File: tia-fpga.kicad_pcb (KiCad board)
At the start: 2 copper layers, 70 x 32 mm, 23 parts, among them J1 PinSocket_1x24_P2.54mm_Vertic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, J2 PinHeader_1x20_P2.54mm_Vertic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, J3 PinHeader_1x20_P2.54mm_Vertic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, J4 PinSocket_1x24_P2.54mm_Vertic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, U1 SOIC-14_3.9x8.7mm_P1.27mm, U2 SOIC-20W_7.5x12.8mm_P1.27mm, U3 SOIC-20W_7.5x12.8mm_P1.27mm, U4 SOIC-20W_7.5x12.8mm_P1.27mm, U5 SOT-23-5, U6 74LVC2G07, U7 74LVC2G07, U8 74LVC2G07, U9 74LVC2G07

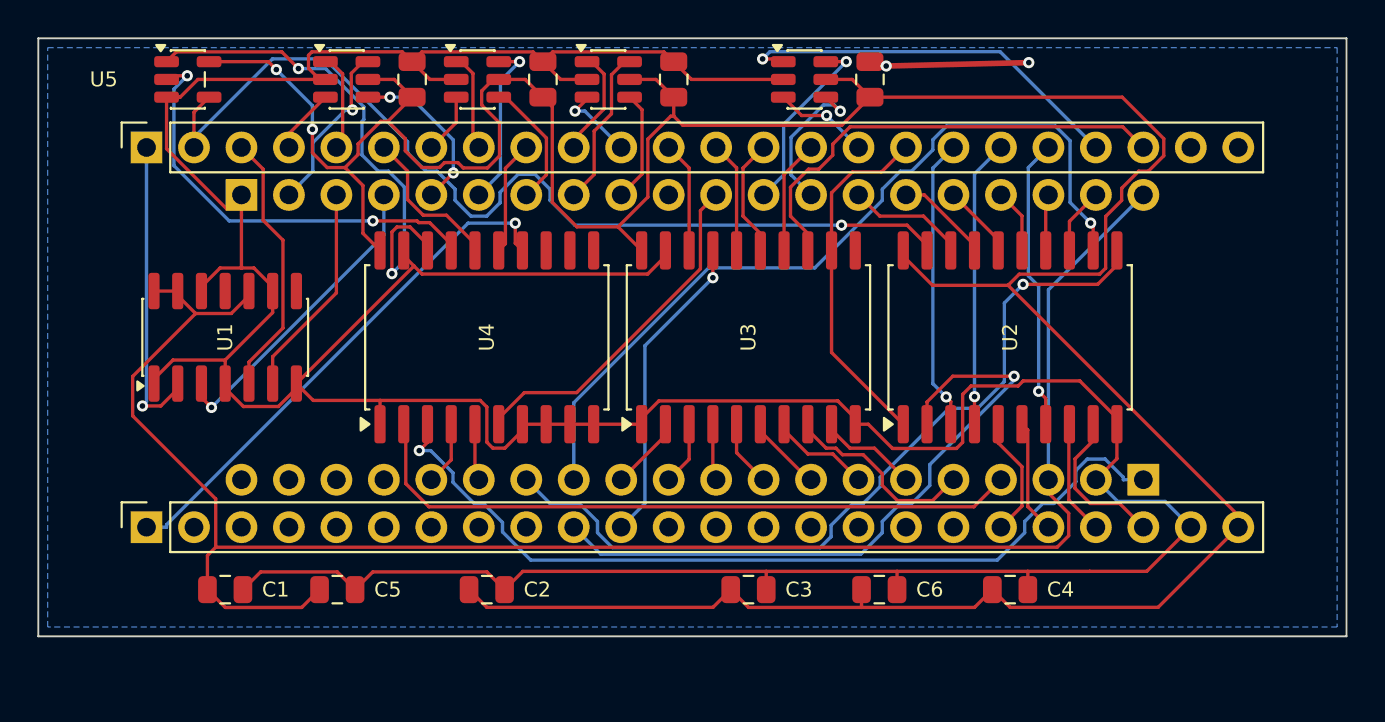
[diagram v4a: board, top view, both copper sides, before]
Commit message: Fix the Tang Nano interface: row spacing, row order, 5 V
Sipeed's dimension drawing for the Tang Nano 9K settles two things this board
had guessed. The module's header rows are 22.86 mm apart, not 20.32, and seen
from above with the USB-C end on the left its J6 row is the upper one -- so the
sockets were the wrong way round as well. J1 now takes J6 and J4 takes J5.
Three sources agree on the order: the pin numbers on the module's underside,
the QN88's own pin order in the top-side photo of Sipeed's datasheet, and
third-party carrier boards for the module. Rev A had both errors too; nothing
was ever fabricated from either.

J1/18, the module's 5 V input, was left open on purpose for breadboard use,
with the Tang Nano powered over USB. In a console that would mean a USB supply
inside the case, so D1 (MBR0540, SOD-123) now feeds it from the TIA socket's
+5 V and blocks the module's USB from feeding the console back.

The board grows 2.54 mm, to 70 x 34.54 mm: J4 moves to y = 28.70 and the
channel's decoupling moves with it, which leaves the top margin as it was. The
pin assignment was solved again for the new geometry (571 mm summed, F_OSC
still on J6/1, the PLL's own input) and the board re-routed: 561 segments, 37
vias, 1.52 m of copper. Freerouting left two ground branches open; each is
closed with a via dropped on the track itself, where it passes over the main
island of the pour. ERC 0; DRC 0 violations, 0 unconnected pads.

Boot time: the console releases the 6507's reset 17 to 58 ms after power-up,
depending on the board revision, and PHI0 has to be running by then. At Gowin's
default 2.5 MHz the GW1NR-9 takes about 100 ms to load its bitstream from
flash, so build_gowin.tcl now asks for -loading_rate 250/8 (31.25 MHz, the
fastest the device allows in Autoboot): about 8 ms. Timing still closes, at
60.4 MHz against the 57.27 MHz clock.

Gerbers, drill, PDFs, renders, both BOMs and the README follow the board.

Co-Authored-By: Claude Opus 5 <noreply@anthropic.com>
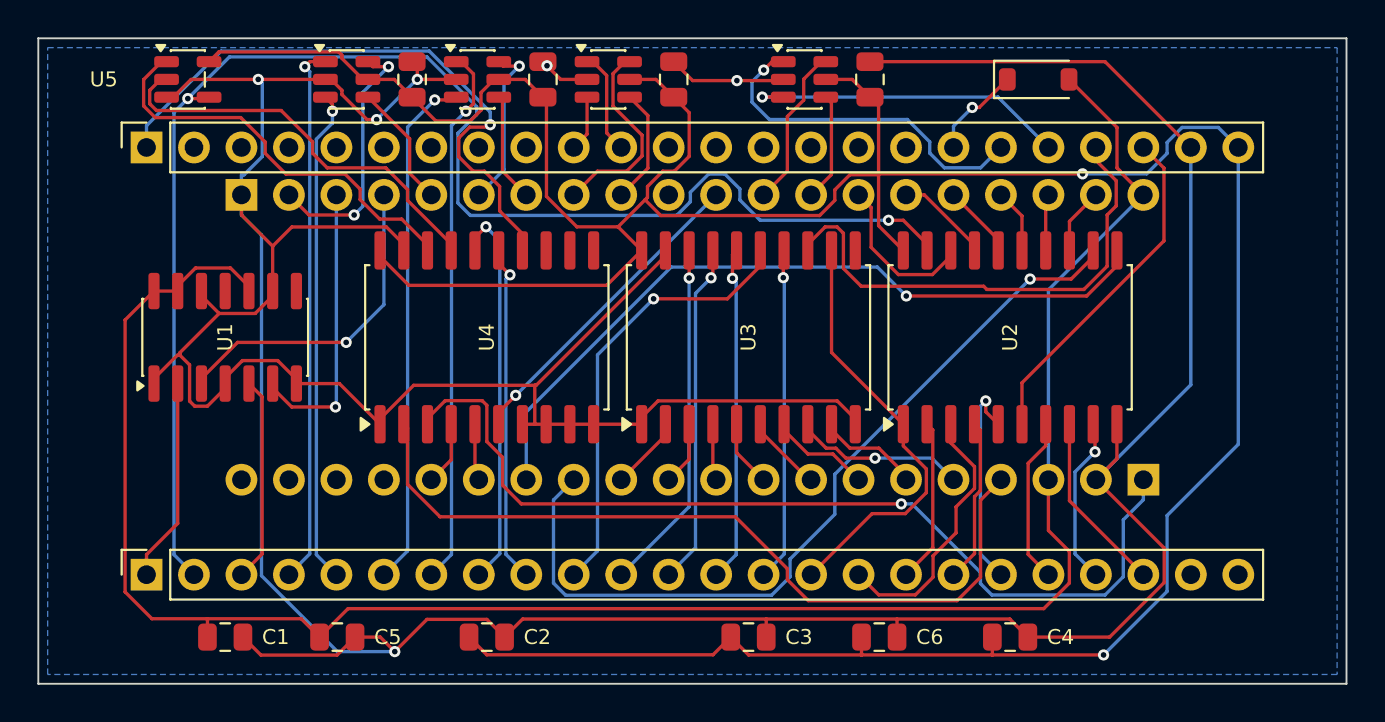
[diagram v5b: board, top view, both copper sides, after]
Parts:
- added D1: MBR0540, D_SOD-123, F.Cu at (53.5, 2.20)
- moved C1 2.54 mm to (10.0, 32.0)
- moved C2 2.54 mm to (24.0, 32.0)
- moved C3 2.54 mm to (38.0, 32.0)
- moved C4 2.54 mm to (52.0, 32.0)
- moved C5 2.54 mm to (16.0, 32.0)
- moved C6 2.54 mm to (45.0, 32.0)
- moved J4 2.54 mm to (5.79, 28.7)
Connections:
- J1 pad 1: /F_PHI0 -> /F_OSC
- J1 pad 10: /F_LUM0 -> /F_COL
- J1 pad 11: /F_COL -> /F_LUM0
- J1 pad 12: /F_A0 -> unconnected-(J1-Pin_12-Pad12)
- J1 pad 13: /F_A2 -> unconnected-(J1-Pin_13-Pad13)
- J1 pad 14: /F_A3 -> unconnected-(J1-Pin_14-Pad14)
- J1 pad 15: /F_A4 -> unconnected-(J1-Pin_15-Pad15)
- J1 pad 16: /F_AU0 -> unconnected-(J1-Pin_16-Pad16)
- J1 pad 17: /F_RW -> unconnected-(J1-Pin_17-Pad17)
- J1 pad 18: /F_D1 -> /TN_5V
- J1 pad 19: /F_D2 -> /F_AU1
- J1 pad 2: /F_CS_N -> unconnected-(J1-Pin_2-Pad2)
- J1 pad 20: /F_D5 -> /F_AU0
- J1 pad 21: /F_AU1 -> /F_A5
- J1 pad 22: /F_A5 -> /F_D4
- J1 pad 23: unconnected-(J1-Pin_23-Pad23) -> GND
- J1 pad 24: unconnected-(J1-Pin_24-Pad24) -> +3V3
- J1 pad 3: /F_RDY -> unconnected-(J1-Pin_3-Pad3)
- J1 pad 4: /F_LUM1 -> unconnected-(J1-Pin_4-Pad4)
- J1 pad 5: /F_CSYNC -> unconnected-(J1-Pin_5-Pad5)
- J1 pad 6: /F_I4 -> unconnected-(J1-Pin_6-Pad6)
- J1 pad 7: /F_LUM2 -> unconnected-(J1-Pin_7-Pad7)
- J1 pad 8: /F_BLK -> unconnected-(J1-Pin_8-Pad8)
- J1 pad 9: /F_I5 -> unconnected-(J1-Pin_9-Pad9)
- J4 pad 1: /F_OSC -> /F_PHI0
- J4 pad 10: /F_D0 -> /F_A3
- J4 pad 11: /F_A1 -> /F_A0
- J4 pad 12: unconnected-(J4-Pin_12-Pad12) -> /F_A1
- J4 pad 13: unconnected-(J4-Pin_13-Pad13) -> /F_A2
- J4 pad 14: unconnected-(J4-Pin_14-Pad14) -> /F_A4
- J4 pad 15: unconnected-(J4-Pin_15-Pad15) -> /F_RW
- J4 pad 16: unconnected-(J4-Pin_16-Pad16) -> /F_D1
- J4 pad 17: unconnected-(J4-Pin_17-Pad17) -> /F_D0
- J4 pad 18: unconnected-(J4-Pin_18-Pad18) -> /F_D2
- J4 pad 2: unconnected-(J4-Pin_2-Pad2) -> /F_CS_N
- J4 pad 20: /F_D4 -> /F_D5
- J4 pad 21: /F_D6 -> /F_D7
- J4 pad 22: /F_D7 -> /F_D6
- J4 pad 23: GND -> unconnected-(J4-Pin_23-Pad23)
- J4 pad 24: +3V3 -> unconnected-(J4-Pin_24-Pad24)
- J4 pad 3: unconnected-(J4-Pin_3-Pad3) -> /F_RDY
- J4 pad 4: unconnected-(J4-Pin_4-Pad4) -> /F_CSYNC
- J4 pad 5: unconnected-(J4-Pin_5-Pad5) -> /F_LUM1
- J4 pad 6: unconnected-(J4-Pin_6-Pad6) -> /F_LUM2
- J4 pad 7: unconnected-(J4-Pin_7-Pad7) -> /F_BLK
- J4 pad 8: unconnected-(J4-Pin_8-Pad8) -> /F_I4
- J4 pad 9: unconnected-(J4-Pin_9-Pad9) -> /F_I5
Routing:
- net /F_CS_N: track 52.2 -> 79.3 mm, vias 1 -> 2
- net /F_D0: track 35.7 -> 8.77 mm, vias 1 -> 0
- net /F_LUM2: track 3.24 -> 27.7 mm, vias 0 -> 1
- net /F_CSYNC: track 5.27 -> 29.0 mm, vias 0 -> 1
- net /F_BLK: track 5.25 -> 28.9 mm, vias 0 -> 1
- net /F_LUM1: track 3.50 -> 26.5 mm, vias 0 -> 1
- net GND: track 229.5 -> 250.2 mm, vias 2 -> 6
- net /F_A3: track 6.35 -> 23.8 mm, vias 0 -> 1
- net /F_A0: track 5.96 -> 18.9 mm, vias 0 -> 1
- net /F_I4: track 8.26 -> 20.9 mm, vias 0 -> 1
- net /F_AU0: track 5.14 -> 17.6 mm
- net /F_D4: track 6.10 -> 18.4 mm
- net /F_I5: track 6.12 -> 18.1 mm, vias 0 -> 1
- net /F_A2: track 5.96 -> 18.0 mm, vias 0 -> 1
- net /F_A4: track 6.11 -> 17.8 mm, vias 0 -> 1
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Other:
- board size 70 x 32 mm -> 70 x 34.5 mm

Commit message: Centre the TIA rows and trim the board to 61.6 mm
The DIP rows sat 1.27 mm off the centre between the module's sockets, left
over from growing the board downwards, and the ends carried more board than
the sockets need. J2, J3 and the channel logic move down 1.27 mm, which leaves
3.81 mm of gap on each side, and the outline loses 8.4 mm: 61.6 x 34.54 mm,
with 0.74 mm of copper to the edge at the ends of the sockets. The board now
reaches about 6.5 mm past the TIA's own pins instead of 10.9.

Re-routed at the new geometry: 534 segments, 39 vias, 1.48 m of copper. The
router left three ground connections open; two took a via on the branch's own
track where it passes over the pour, and the last two capacitors are tied to
their neighbours along the free lane just inside the top edge. The pour is
smaller and in two islands now (759 mm2), since the board is narrower and the
routing denser, but every ground item is connected. U5's designator moves to
the back silkscreen, where the other top-margin parts already keep theirs.
ERC 0; DRC 0 violations, 0 unconnected pads.

Gerbers, drill, the PCB PDF, renders, the fabrication notes and the README
follow the board.

Co-Authored-By: Claude Opus 5 <noreply@anthropic.com>
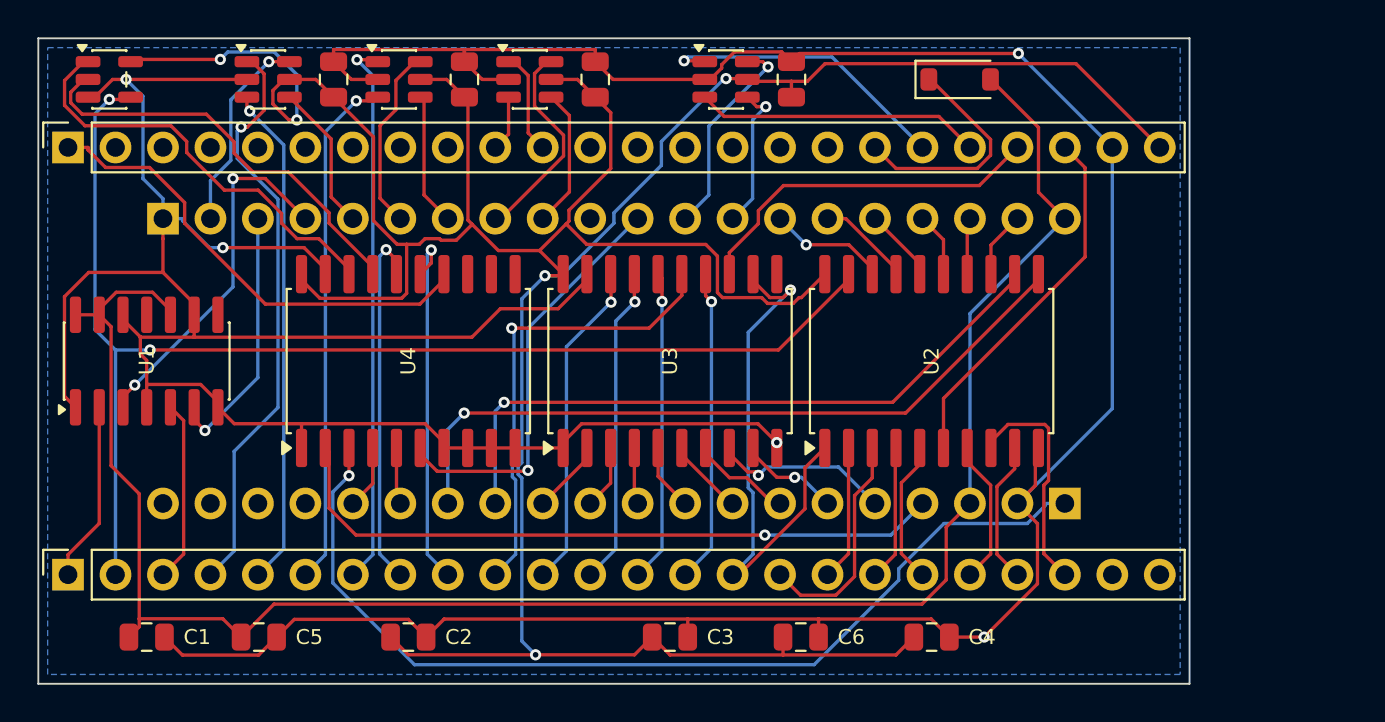
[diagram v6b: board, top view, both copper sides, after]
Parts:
- moved J3 4.39 mm to (54.9, 24.9)
- moved U2 4.39 mm to (47.8, 17.3)
- moved U3 4.39 mm to (33.8, 17.3)
- moved U1 4.39 mm to (5.80, 17.3)
- moved J2 4.39 mm to (6.67, 9.65)
- moved U4 4.39 mm to (19.8, 17.3)
- moved C10 4.20 mm to (40.3, 2.20)
- moved C3 4.20 mm to (33.8, 32.0)
- moved C4 4.20 mm to (47.8, 32.0)
- moved C6 4.20 mm to (40.8, 32.0)
- moved D1 4.20 mm to (49.3, 2.20)
- moved U9 4.20 mm to (36.8, 2.20)
- moved C1 4.20 mm to (5.80, 32.0)
- moved J1 4.20 mm to (1.59, 5.84)
- moved J4 4.20 mm to (1.59, 28.7)
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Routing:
- net /F_CS_N: track 79.3 -> 68.5 mm
- net /TIA_D6: track 44.8 -> 36.0 mm
- net /F_OSC: track 33.0 -> 25.2 mm, vias 1 -> 0
- net /F_A5: track 26.7 -> 19.3 mm
- net /TN_5V: track 5.05 -> 12.4 mm, vias 1 -> 0
- net +5V: track 108.0 -> 100.7 mm
- net /TIA_CS0_N: track 43.1 -> 36.4 mm, vias 0 -> 1
- net +3V3: track 175.0 -> 181.5 mm, vias 2 -> 5
- net /F_RW: track 23.0 -> 28.7 mm, vias 0 -> 1
- net /TIA_OSC: track 17.1 -> 22.4 mm
- net /F_D3: track 11.4 -> 7.66 mm, vias 1 -> 0
- net /TIA_CSYNC: track 13.8 -> 10.8 mm, vias 2 -> 1
- net /F_AU1: track 18.8 -> 16.0 mm
- net /F_D6: track 9.69 -> 12.3 mm
- net /TIA_AU1: track 8.65 -> 11.2 mm, vias 0 -> 1
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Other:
- board size 70 x 34.5 mm -> 61.6 x 34.5 mm

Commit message: Put the licence notice on the back silkscreen
CERN-OHL-S v2 asks for the notice to travel with the board, and until now it
lived only in the files. The back silkscreen carries CERN-OHL-S v2, LRRosa 2026
and github.com/lrrosa/tia-fpga, centred between the two rows of TIA pins, where
the back had neither silk nor pads.

DRC stays at 0 violations and 0 unconnected pads. Gerbers, drill, the PCB PDF
and both renders follow; the fabrication notes and the README ask for the
notice to be kept on a respin.

Co-Authored-By: Claude Opus 5 <noreply@anthropic.com>
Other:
- board text added: "CERN-OHL-S v2"
- board text added: "LRRosa 2026"
- board text added: "github.com/lrrosa/tia-fpga"
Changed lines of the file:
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@@
 		(layer "Edge.Cuts")
+	)
+	(gr_text "github.com/lrrosa/tia-fpga"
+		(at 30.8 20.54 0)
+		(layer "B.SilkS")
+		(effects
+			(font
+				(size 1.3 1.3)
+				(thickness 0.2)
+			)
+			(justify mirror)
+		)
+	)
+	(gr_text "LRRosa 2026"
+		(at 30.8 14 0)
+		(layer "B.SilkS")
+		(effects
+			(font
+				(size 1.4 1.4)
+				(thickness 0.2)
+			)
+			(justify mirror)
+		)
+	)
+	(gr_text "CERN-OHL-S v2"
+		(at 30.8 17.27 0)
+		(layer "B.SilkS")
+		(effects
+			(font
+				(size 1.4 1.4)
+				(thickness 0.2)
+			)
+			(justify mirror)
+		)
 	)
 	(segment

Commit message: Mark pin 1 and the keyed end on the silkscreen
The board went out with no way to tell which end of the DIP row is pin 1. The
back now carries a half moon at the end where the TIA's pin 1 and pin 40 sit,
keyed the way the chip's own package is, and the numbers 1, 20, 21 and 40
beside the corner pads; the front repeats 1 and 40. The front cannot take the
half moon: U1's own outline is in that corner.

DRC stays at 0 violations and 0 unconnected pads. Gerbers, drill, the PCB PDF,
both renders, the fabrication notes and the README follow.

Co-Authored-By: Claude Opus 5 <noreply@anthropic.com>
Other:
- board text added: "1"
- board text added: "20"
- board text added: "21"
- board text added: "40"
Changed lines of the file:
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@@
+	)
+	(gr_line
+		(start 0.947703 17.632346)
+		(end 0.899999 17.27)
+		(stroke
+			(width 0.15)
+			(type default)
+		)
+		(layer "B.SilkS")
+	)
+	(gr_line
+		(start 1.087564 17.97)
+		(end 0.947703 17.632346)
+		(stroke
+			(width 0.15)
+			(type default)
+		)
+		(layer "B.SilkS")
+	)
+	(gr_line
+		(start 1.31005 18.259949)
+		(end 1.087564 17.97)
+		(stroke
+			(width 0.15)
+			(type default)
+		)
+		(layer "B.SilkS")
+	)
+	(gr_line
+		(start 1.599999 18.482435)
+		(end 1.31005 18.259949)
+		(stroke
+			(width 0.15)
+			(type default)
+		)
+		(layer "B.SilkS")
+	)
+	(gr_line
+		(start 1.937653 18.622296)
+		(end 1.599999 18.482435)
+		(stroke
+			(width 0.15)
+			(type default)
+		)
+		(layer "B.SilkS")
+	)
+	(gr_line
+		(start 2.3 18.67)
+		(end 1.937653 18.622296)
+		(stroke
+			(width 0.15)
+			(type default)
+		)
+		(layer "B.SilkS")
+	)
+	(gr_line
+		(start 2.662346 18.622296)
+		(end 2.3 18.67)
+		(stroke
+			(width 0.15)
+			(type default)
+		)
+		(layer "B.SilkS")
+	)
+	(gr_line
+		(start 2.999999 18.482435)
+		(end 2.662346 18.622296)
+		(stroke
+			(width 0.15)
+			(type default)
+		)
+		(layer "B.SilkS")
+	)
+	(gr_line
+		(start 3.289949 18.259949)
+		(end 2.999999 18.482435)
+		(stroke
+			(width 0.15)
+			(type default)
+		)
+		(layer "B.SilkS")
+	)
+	(gr_line
+		(start 3.512435 17.97)
+		(end 3.289949 18.259949)
+		(stroke
+			(width 0.15)
+			(type default)
+		)
+		(layer "B.SilkS")
+	)
+	(gr_line
+		(start 3.652296 17.632346)
+		(end 3.512435 17.97)
+		(stroke
+			(width 0.15)
+			(type default)
+		)
+		(layer "B.SilkS")
+	)
+	(gr_line
+		(start 3.699999 17.27)
+		(end 0.899999 17.27)
+		(stroke
+			(width 0.15)
+			(type default)
+		)
+		(layer "B.SilkS")
+	)
+	(gr_line
+		(start 3.699999 17.27)
+		(end 3.652296 17.632346)
+		(stroke
+			(width 0.15)
+			(type default)
+		)
+		(layer "B.SilkS")
 	)
 	(gr_line
@@
 		(layer "Edge.Cuts")
 	)
+	(gr_text "1"
+		(at 6.67 11.55 0)
+		(layer "F.SilkS")
+		(effects
+			(font
+				(size 1.2 1.2)
+				(thickness 0.18)
+			)
+		)
+	)
+	(gr_text "40"
+		(at 6.67 22.99 0)
+		(layer "F.SilkS")
+		(effects
+			(font
+				(size 1.2 1.2)
+				(thickness 0.18)
+			)
+		)
+	)
+	(gr_text "1"
+		(at 6.67 12.1 0)
+		(layer "B.SilkS")
+		(effects
+			(font
+				(size 1.2 1.2)
+				(thickness 0.18)
+			)
+			(justify mirror)
+		)
+	)
+	(gr_text "40"
+		(at 6.67 22.4 0)
+		(layer "B.SilkS")
+		(effects
+			(font
+				(size 1.2 1.2)
+				(thickness 0.18)
+			)
+			(justify mirror)
+		)
+	)
+	(gr_text "20"
+		(at 54.93 12.1 0)
+		(layer "B.SilkS")
+		(effects
+			(font
+				(size 1.2 1.2)
+				(thickness 0.18)
+			)
+			(justify mirror)
+		)
+	)
+	(gr_text "21"
+		(at 54.93 22.4 0)
+		(layer "B.SilkS")
+		(effects
+			(font
+				(size 1.2 1.2)
+				(thickness 0.18)
+			)
+			(justify mirror)
+		)
+	)
 	(gr_text "github.com/lrrosa/tia-fpga"
